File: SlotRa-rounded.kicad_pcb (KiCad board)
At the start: 2 copper layers, 35 x 44 mm, 30 parts, among them J1 PinsBatt, J2 Conn_Out_Ext, J3 ControllerL, J4 ModemL, J5 ControllerR, J6 ModemR, J7 Conn_GPS, J8 Conn_I2C, SW1 ButRst, SW2 ButUsr, T1 SI2312, U1 XB8089D0

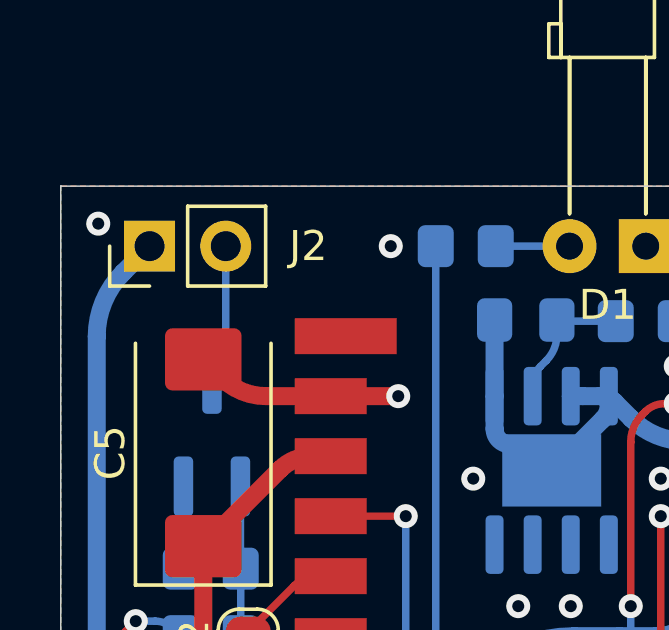
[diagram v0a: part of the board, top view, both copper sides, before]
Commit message: Quick Fix: MOSFET line
Just a quick fix: T1 Drain circuit was too thin. It's in the Power family now, so the line is thick.
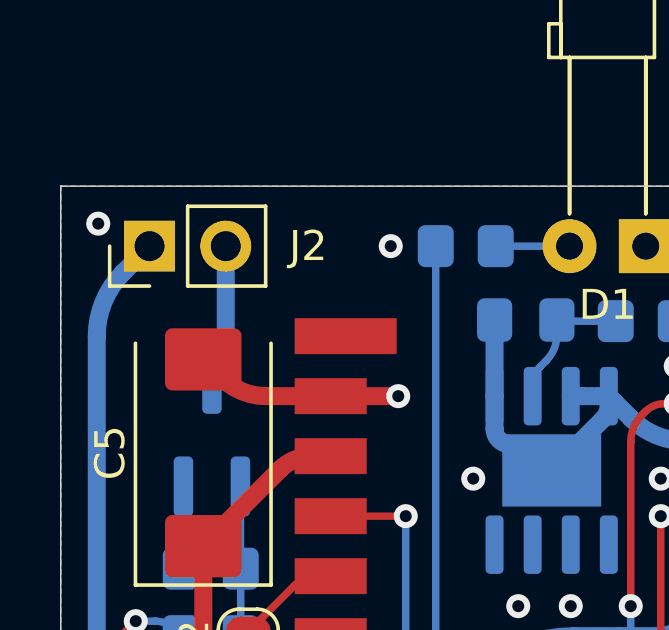
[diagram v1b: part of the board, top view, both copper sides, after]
